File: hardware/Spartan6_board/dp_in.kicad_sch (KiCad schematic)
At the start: 26 parts, among them J10 TF TF-018 1.5mm, J4 HDMI_A, J9 Conn_01x20, Q3 AO3400A, Q4 AO3400A, Q5 AO3400A

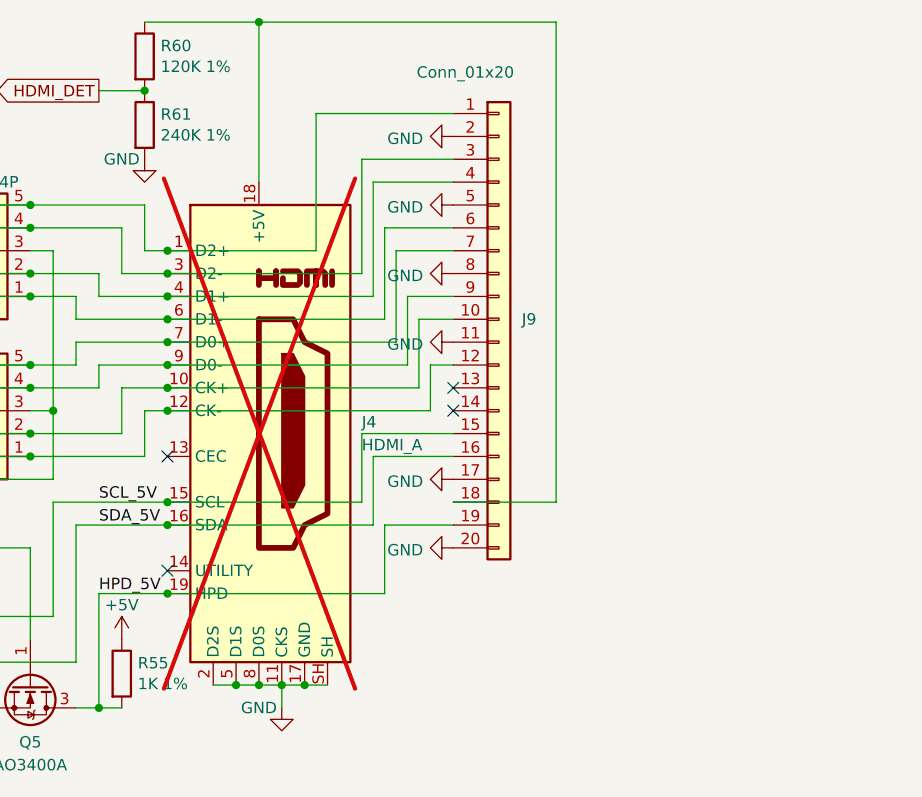
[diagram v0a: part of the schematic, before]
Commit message: change DVI FPC pinout to match DVI connector (G-S-S-G), and FPGA device from XC6SLX16-FTG256 to XC6SLX25-3FTG256C
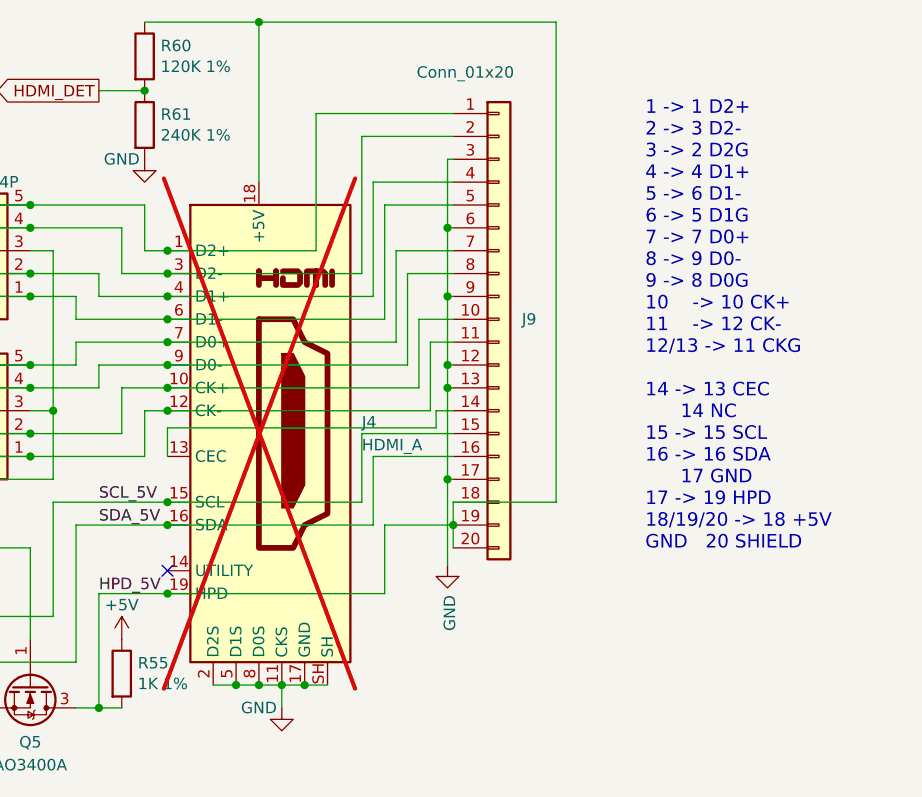
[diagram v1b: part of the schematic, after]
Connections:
- net GND: now also J9.12 (Pin_12), J9.13 (Pin_13), J9.3 (Pin_3), J9.6 (Pin_6), J9.9 (Pin_9); no longer J9.11 (Pin_11), J9.2 (Pin_2), J9.20 (Pin_20), J9.5 (Pin_5), J9.8 (Pin_8)
- net HPD_5V: now also J4.18 (+5V), J9.18 (Pin_18), J9.20 (Pin_20), R60.1
- net TMDS_CKN: now also J9.11 (Pin_11); no longer J9.12 (Pin_12)
- net TMDS_D0N: now also J9.8 (Pin_8); no longer J9.9 (Pin_9)
- net TMDS_D1N: now also J9.5 (Pin_5); no longer J9.6 (Pin_6)
- net TMDS_D2N: now also J9.2 (Pin_2); no longer J9.3 (Pin_3)
- net at J4.13 (CEC): now also J9.14 (Pin_14)
- no-connect marks 4 -> 1
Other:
- note added: "1 -> 1 D2+ 2 -> 3 D2- 3 -> 2 D2G 4 -> 4 D1+ 5 -> 6 D1- 6 -> 5 D1G 7 -> 7 D0+ 8 -> 9 D0- 9 -> 8 D0G 10 -> 10 CK+ 11 -> 12 CK- 12/13 -> 11 CKG 14 -> 13 CEC 14 NC 15 -> 15 SCL 16 -> 16 SDA 17 GND 17 -> 19 HPD 18/19/20 -> 18 +5V GND 20 SHIELD"
- company: Copyright 2022 Modos / Engineer: Wenting Zhang -> (C) 2026 Victor Suarez Rovere
- title: Caster EPDC -> Spartan 6 FPGA board

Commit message: review and update manufacturing constraints (via size, etc.)
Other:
- company: (C) 2026 Victor Suarez Rovere -> (C) 2025-2026 Victor Suarez Rovere <suarezvictor@gmail.com>
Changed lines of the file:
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@@
 	(title_block
 		(title "Spartan 6 FPGA board")
-		(date "2026-09-17")
+		(date "2026-09-18")
 		(rev "R0.1")
-		(company "(C) 2026 Victor Suarez Rovere")
-		(comment 1 "(C) 2022 Modos / Engineer: Wenting Zhang (Caster EPDC)")
+		(company "(C) 2025-2026 Victor Suarez Rovere <suarezvictor@gmail.com>")
+		(comment 1 "Copyright 2023 Modos / Engineer: Wenting Zhang")
 	)
 	(junction
